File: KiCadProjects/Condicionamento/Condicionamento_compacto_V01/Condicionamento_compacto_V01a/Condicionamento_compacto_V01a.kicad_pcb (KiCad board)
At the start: 2 copper layers, 45 x 33 mm, 19 parts, among them J1 Entrada, J2 Canais, J3 Conn_01x02, J4 Conn_01x02, U1-Cond1 AD828AN

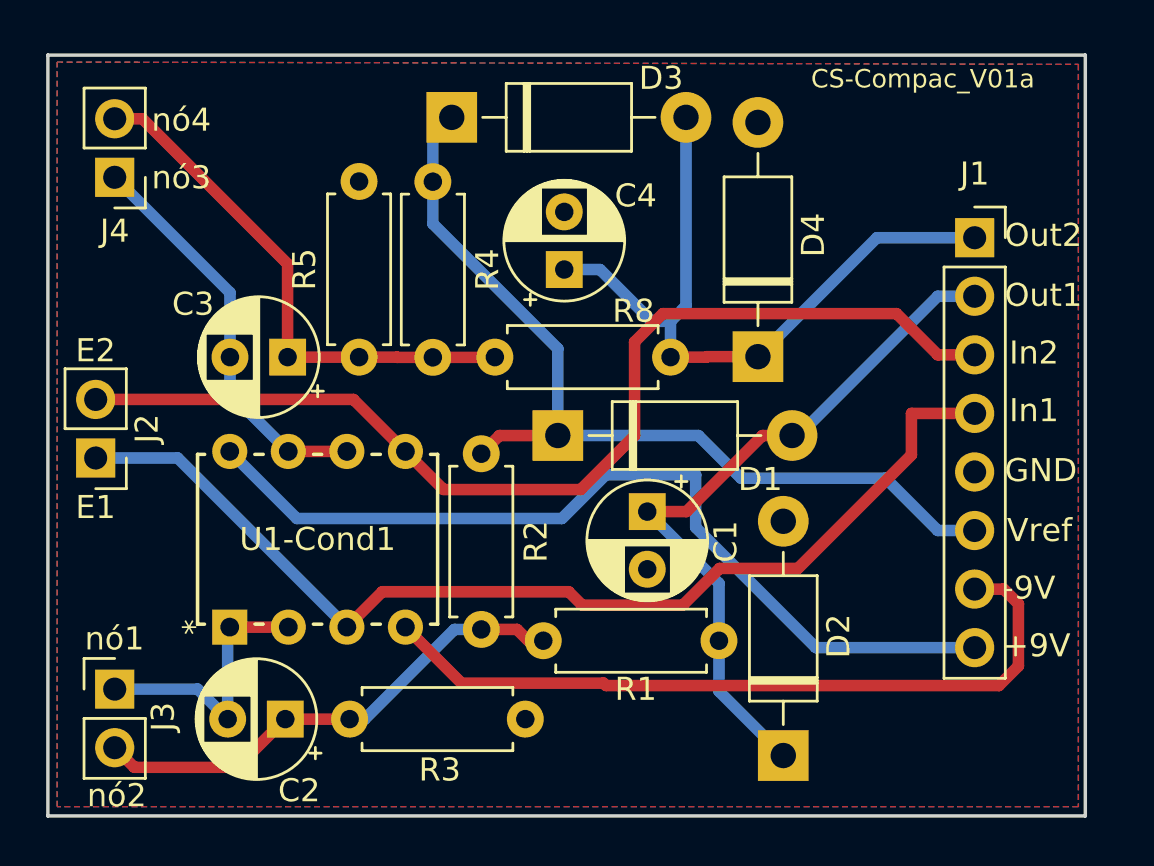
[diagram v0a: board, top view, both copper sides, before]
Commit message: V01aCopia: menor, com vias. V01a: maior, sem vias
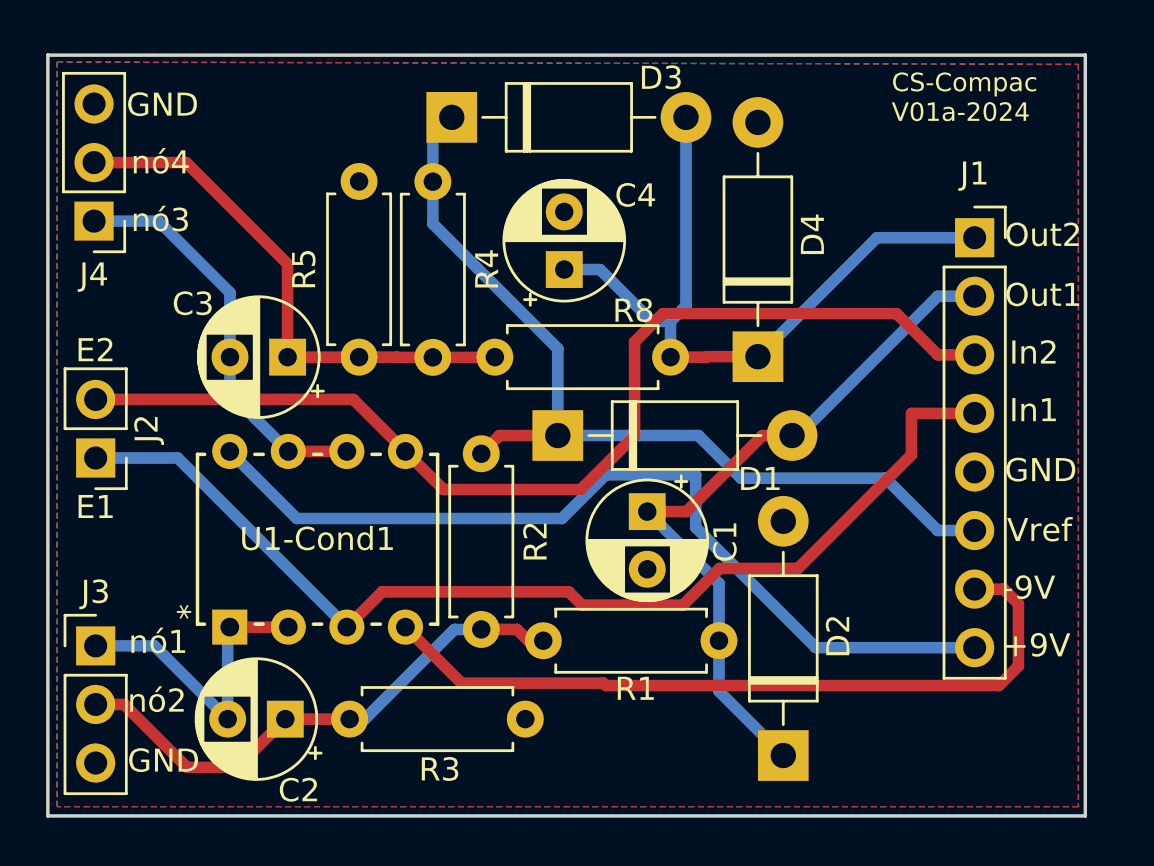
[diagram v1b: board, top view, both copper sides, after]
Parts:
- J3, J4: value Conn_01x02 -> Conn_01x03; footprint Connector_PinHeader_2.54mm:PinHeader_1x02_P2.54mm_Vertical -> Connector_PinHeader_2.54mm:PinHeader_1x03_P2.54mm_Vertical
- moved J4 2.10 mm to (124.1, 92.3)
- moved J3 2.05 mm to (124.2, 110.7)
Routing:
- net nó2: track 21.6 -> 23.2 mm
- net nó1: track 12.0 -> 13.6 mm
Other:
- board text added: "CS-Compac V01a-2024"
- board text removed: "CS-Compac_V01a"

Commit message: lista de materiais
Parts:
- moved C2 26.0 mm to (130.3, 88.0), turned to -45 degrees
- moved R3 16.9 mm to (149.0, 104.2)
- moved R1 16.3 mm to (156.7, 100.8), turned to 180 degrees
- moved D1 11.6 mm to (155.2, 97.7), turned to 90 degrees
- moved J3 8.28 mm to (124.1, 102.5)
- moved D2 7.83 mm to (154.1, 107.7), turned to 180 degrees
- moved C1 4.91 mm to (145.2, 100.9)
- moved J1 4.67 mm to (162.0, 88.4)
- moved J2 3.95 mm to (124.1, 98.6)
- moved D3 3.00 mm to (136.6, 87.8)
- moved R2 1.85 mm to (140.9, 100.5)
- moved U1-Cond1 1.85 mm to (129.9, 108.1)
- moved C3 1.65 mm to (132.4, 96.5)
- moved D4 1.16 mm to (151.8, 97.7)
- moved C4 1.10 mm to (143.4, 94.4)
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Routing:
- net nó2: track 23.2 -> 55.0 mm, vias 0 -> 1
- net Canal_2: track 46.0 -> 65.5 mm
- net Out_1: track 31.1 -> 47.6 mm
- net nó1: track 13.6 -> 27.8 mm
- net Vref: track 39.8 -> 53.7 mm
- net +9V: track 38.7 -> 45.5 mm
- net -9V: track 32.9 -> 26.3 mm
- net nó3: track 17.7 -> 15.1 mm
- net Out_2: track 31.6 -> 34.1 mm, vias 0 -> 1
- net Canal_1: track 46.5 -> 47.9 mm
- net nó4: track 23.3 -> 21.9 mm
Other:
- board size 45 x 33 mm -> 45 x 25 mm
